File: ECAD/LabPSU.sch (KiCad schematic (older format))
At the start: 55 parts, among them J1 PWR, U1 LM358

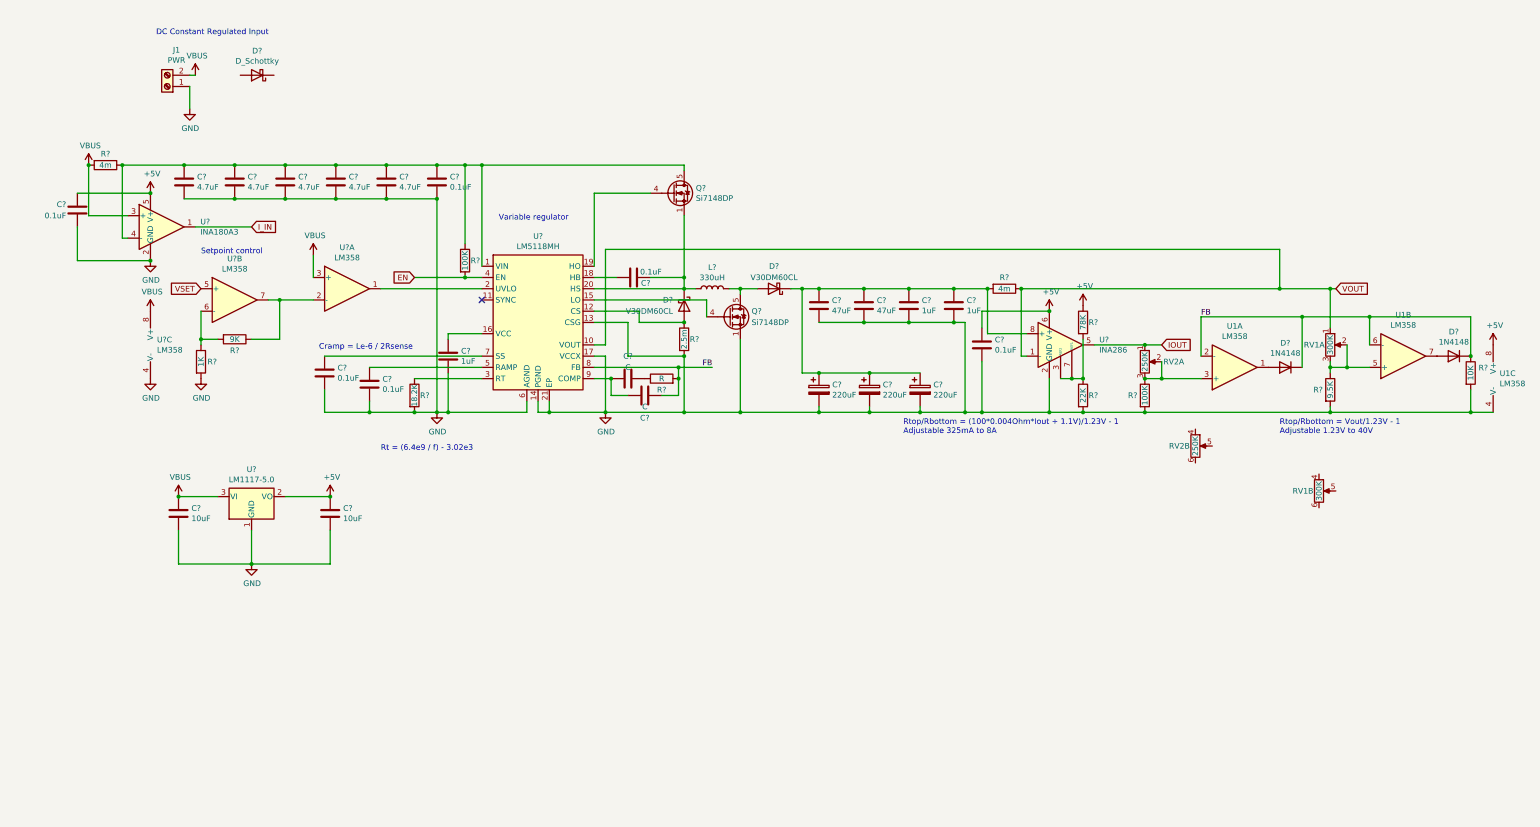
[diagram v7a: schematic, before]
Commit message: select diode and compensation network
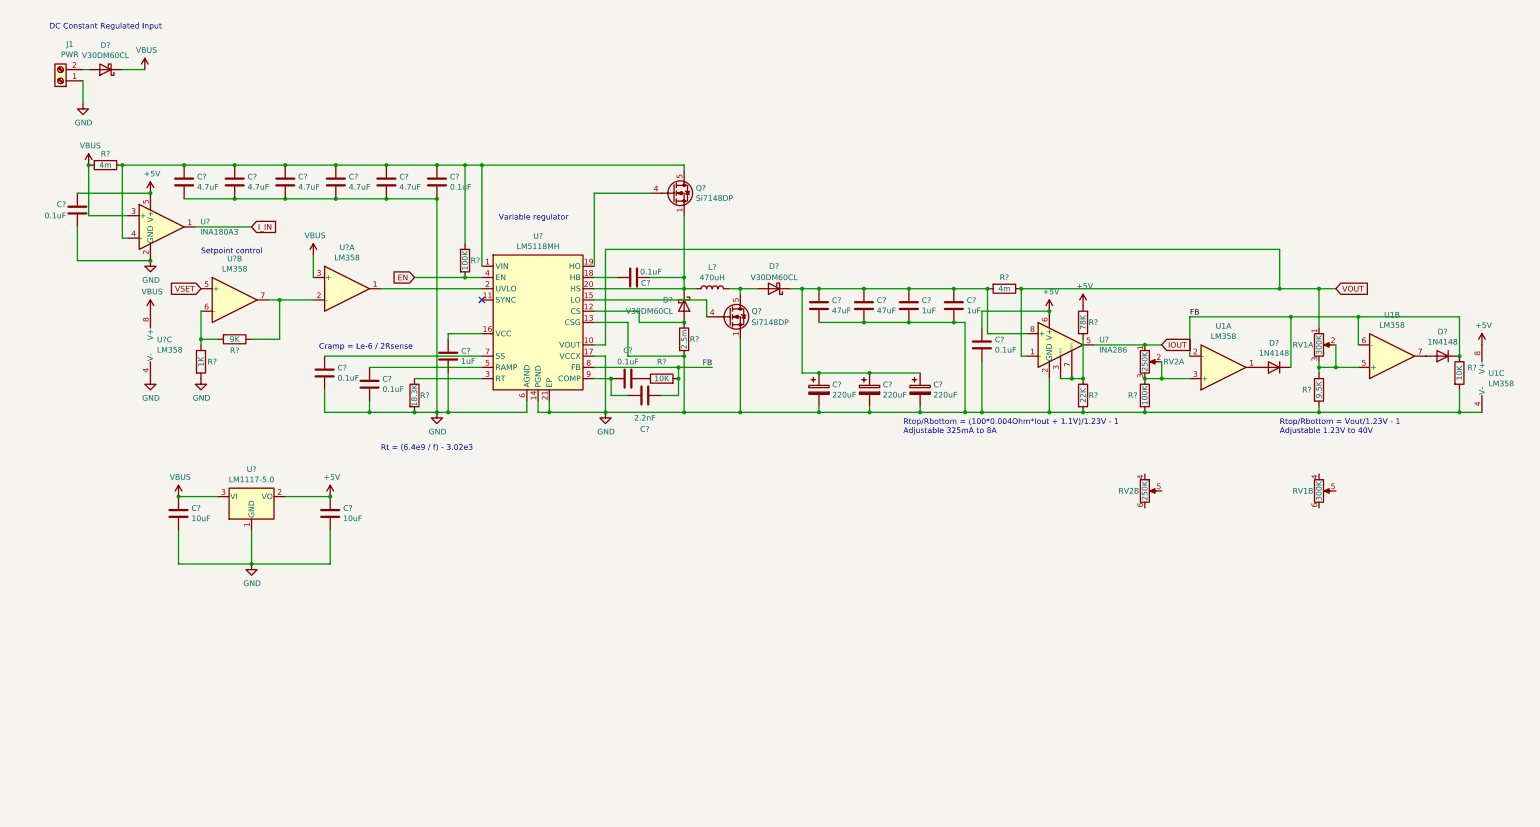
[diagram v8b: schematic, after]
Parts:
- C?: value C -> 0.1uF
- C?: value C -> 2.2nF
- D?: value D_Schottky -> V30DM60CL
- L?: value 330uH -> 470uH
- R?: value 18.2K -> 18.3K
- R?: value R -> 10K
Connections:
- net VBUS: now also D?.1 (K); no longer J1.2 (Pin_2)
- net at D?.2 (A): now also J1.2 (Pin_2)
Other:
- moved on the sheet: D?, J1, R?, RV1A, RV2B, U1A, U1B, U1C
